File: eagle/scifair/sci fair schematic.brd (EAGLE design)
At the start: 45.4 x 80 mm, 19 parts, among them IC1 LM555N, IC2 LM340H-12, Q1 BC817-16W, Q2 BC817-16W, X1 RIGHT, X2 LEFT, X3 PWR

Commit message: Rework USB connections to use Sparkfun breakouts due to resource unavailability
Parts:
- removed X1: RIGHT, con-yamaichi:USB-A003
- removed X2: LEFT, con-yamaichi:USB-A003
- removed X3: PWR, con-yamaichi:USB-A003
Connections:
- net N$6 renamed 5V
- removed net N$1: C2.1, IC2.1, X1.4, X2.4, X3.3
- removed net N$2: F1.1, X2.3
- removed net N$3: F2.1, X1.3
- new net VCC: C2.1, F1.1, F2.1, IC2.1
- net GND: no longer X3.4
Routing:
- net N$1: track 97.1 -> 0.00 mm, vias 1 -> 0
- net VCC: track 0.00 -> 25.3 mm, vias 0 -> 2
- net N$2: track 15.5 -> 0.00 mm
- net N$3: track 12.9 -> 0.00 mm, vias 2 -> 0
- net GND: track 131.3 -> 122.6 mm, vias 7 -> 5
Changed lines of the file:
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@@
 <attribute name="VALUE" x="60.96" y="71.374" size="1.27" layer="27" ratio="10" rot="R90"/>
-</element>
-<element name="X1" library="con-yamaichi" package="USB-A003" value="RIGHT" x="107.95" y="35.56" smashed="yes" rot="R90">
-<attribute name="OC_FARNELL" value="unknown" x="107.95" y="35.56" size="1.778" layer="27" rot="R90" display="off"/>
-<attribute name="MPN" value="" x="107.95" y="35.56" size="1.778" layer="27" rot="R90" display="off"/>
-<attribute name="MF" value="" x="107.95" y="35.56" size="1.778" layer="27" rot="R90" display="off"/>
-<attribute name="OC_NEWARK" value="unknown" x="107.95" y="35.56" size="1.778" layer="27" rot="R90" display="off"/>
-<attribute name="NAME" x="96.52" y="27.94" size="1.27" layer="25" rot="R180"/>
-<attribute name="VALUE" x="99.06" y="45.72" size="1.27" layer="27" rot="R180"/>
-</element>
-<element name="X2" library="con-yamaichi" package="USB-A003" value="LEFT" x="107.95" y="57.15" smashed="yes" rot="R90">
-<attribute name="OC_FARNELL" value="unknown" x="107.95" y="57.15" size="1.778" layer="27" rot="R90" display="off"/>
-<attribute name="MPN" value="" x="107.95" y="57.15" size="1.778" layer="27" rot="R90" display="off"/>
-<attribute name="MF" value="" x="107.95" y="57.15" size="1.778" layer="27" rot="R90" display="off"/>
-<attribute name="OC_NEWARK" value="unknown" x="107.95" y="57.15" size="1.778" layer="27" rot="R90" display="off"/>
-<attribute name="NAME" x="96.52" y="49.53" size="1.27" layer="25" rot="R180"/>
-<attribute name="VALUE" x="96.52" y="66.04" size="1.27" layer="27" rot="R180"/>
-</element>
-<element name="X3" library="con-yamaichi" package="USB-A003" value="PWR" x="90.17" y="86.36" smashed="yes" rot="R180">
-<attribute name="OC_FARNELL" value="unknown" x="90.17" y="86.36" size="1.778" layer="27" rot="R180" display="off"/>
-<attribute name="MPN" value="" x="90.17" y="86.36" size="1.778" layer="27" rot="R180" display="off"/>
-<attribute name="MF" value="" x="90.17" y="86.36" size="1.778" layer="27" rot="R180" display="off"/>
-<attribute name="OC_NEWARK" value="unknown" x="90.17" y="86.36" size="1.778" layer="27" rot="R180" display="off"/>
-<attribute name="NAME" x="95.25" y="71.12" size="1.27" layer="25" rot="R270"/>
-<attribute name="VALUE" x="80.01" y="78.74" size="1.27" layer="27" rot="R270"/>
 </element>
 <element name="LED3" library="led" package="LED3MM" value="TLLY4400" x="87.63" y="60.96" smashed="yes">
@@
 </elements>
 <signals>
-<signal name="N$1">
-<contactref element="X3" pad="3"/>
-<contactref element="X1" pad="4"/>
-<contactref element="X2" pad="4"/>
-<contactref element="IC2" pad="1"/>
-<contactref element="C2" pad="1"/>
-<wire x1="74.93" y1="20.32" x2="74.93" y2="16.51" width="0.4064" layer="16"/>
-<wire x1="74.93" y1="16.51" x2="78.74" y2="16.51" width="0.4064" layer="16"/>
-<wire x1="78.74" y1="16.51" x2="81.915" y2="13.335" width="0.4064" layer="16"/>
-<wire x1="93.95" y1="39.06" x2="91.13" y2="39.06" width="0.4064" layer="1"/>
-<wire x1="91.13" y1="39.06" x2="91.44" y2="38.1" width="0.4064" layer="1"/>
-<wire x1="91.44" y1="38.1" x2="91.44" y2="21.59" width="0.4064" layer="1"/>
-<wire x1="91.44" y1="21.59" x2="81.915" y2="13.335" width="0.4064" layer="1"/>
-<via x="81.915" y="13.335" extent="1-16" drill="0.6" shape="square"/>
-<wire x1="81.915" y1="13.335" x2="85.09" y2="10.16" width="0.4064" layer="16"/>
-<wire x1="93.95" y1="60.65" x2="93.95" y2="64.8" width="0.4064" layer="1"/>
-<wire x1="93.95" y1="64.8" x2="88.9" y2="69.85" width="0.4064" layer="1"/>
-<wire x1="88.9" y1="69.85" x2="88.9" y2="72.09" width="0.4064" layer="1"/>
-<wire x1="88.9" y1="72.09" x2="89.17" y2="72.36" width="0.4064" layer="1"/>
-<wire x1="93.95" y1="60.65" x2="96.83" y2="60.65" width="0.4064" layer="1"/>
-<wire x1="96.83" y1="60.65" x2="100.33" y2="57.15" width="0.4064" layer="1"/>
-<wire x1="100.33" y1="57.15" x2="100.33" y2="38.1" width="0.4064" layer="1"/>
-<wire x1="100.33" y1="38.1" x2="94.91" y2="38.1" width="0.4064" layer="1"/>
-<wire x1="94.91" y1="38.1" x2="93.95" y2="39.06" width="0.4064" layer="1"/>
-</signal>
-<signal name="N$2">
-<contactref element="X2" pad="3"/>
-<contactref element="F1" pad="1"/>
-<wire x1="93.95" y1="58.15" x2="91.17" y2="58.15" width="0.4064" layer="1"/>
-<wire x1="91.17" y1="58.15" x2="90.17" y2="57.15" width="0.4064" layer="1"/>
-<wire x1="90.17" y1="57.15" x2="90.17" y2="45.85" width="0.4064" layer="1"/>
-</signal>
-<signal name="N$3">
-<contactref element="X1" pad="3"/>
-<contactref element="F2" pad="1"/>
-<wire x1="93.95" y1="36.56" x2="94.22" y2="36.83" width="0.4064" layer="1"/>
-<wire x1="94.22" y1="36.83" x2="97.79" y2="36.83" width="0.4064" layer="1"/>
-<via x="97.79" y="36.83" extent="1-16" drill="0.6" shape="square"/>
-<via x="93.98" y="40.64" extent="1-16" drill="0.6" shape="square"/>
-<wire x1="93.98" y1="40.64" x2="93.98" y2="43.05" width="0.4064" layer="1"/>
-<wire x1="93.98" y1="40.64" x2="97.79" y2="39.37" width="0.4064" layer="16"/>
-<wire x1="97.79" y1="39.37" x2="97.79" y2="36.83" width="0.4064" layer="16"/>
-</signal>
 <signal name="N$4">
 <contactref element="Q1" pad="2"/>
@@
 </signal>
 <signal name="GND">
-<contactref element="X3" pad="4"/>
 <contactref element="IC2" pad="2"/>
 <contactref element="C2" pad="2"/>
@@
 <wire x1="77.47" y1="75.6412" x2="77.47" y2="71.12" width="0.4064" layer="16"/>
 <via x="77.47" y="71.12" extent="1-16" drill="0.6" shape="square"/>
-<wire x1="85.43" y1="71.12" x2="86.67" y2="72.36" width="0.4064" layer="1"/>
 <wire x1="68.58" y1="36.83" x2="66.294" y2="36.83" width="0.4064" layer="16"/>
 <wire x1="66.294" y1="36.83" x2="62.484" y2="33.02" width="0.4064" layer="16"/>
@@
 <wire x1="87.63" y1="17.78" x2="85.09" y2="20.32" width="0.4064" layer="16"/>
 <wire x1="85.09" y1="20.32" x2="80.01" y2="20.32" width="0.4064" layer="16"/>
-<wire x1="86.67" y1="72.36" x2="86.67" y2="69.54" width="0.4064" layer="1"/>
 <wire x1="86.67" y1="69.54" x2="88.9" y2="67.31" width="0.4064" layer="1"/>
 <via x="88.9" y="67.31" extent="1-16" drill="0.6" shape="square"/>
@@
 <via x="81.28" y="54.61" extent="1-16" drill="0.6" shape="square"/>
 <wire x1="81.28" y1="54.61" x2="81.28" y2="57.15" width="0.4064" layer="16"/>
-<via x="81.28" y="71.12" extent="1-16" drill="0.6" shape="square"/>
-<wire x1="81.28" y1="71.12" x2="77.47" y2="71.12" width="0" layer="19" extent="1-1"/>
-<wire x1="81.28" y1="71.12" x2="83.82" y2="71.12" width="0.4064" layer="16"/>
-<via x="83.82" y="71.12" extent="1-16" drill="0.6" shape="square"/>
-<wire x1="83.82" y1="71.12" x2="85.43" y2="71.12" width="0.4064" layer="1"/>
-</signal>
-<signal name="N$6">
+<wire x1="86.67" y1="69.54" x2="77.47" y2="71.12" width="0" layer="19" extent="1-1"/>
+</signal>
+<signal name="5V">
 <contactref element="IC2" pad="3"/>
 <contactref element="C3" pad="1"/>
@@
 <wire x1="86.36" y1="60.96" x2="86.36" y2="64.77" width="0.4064" layer="16"/>
 </signal>
+<signal name="VCC">
+<contactref element="C2" pad="1"/>
+<contactref element="IC2" pad="1"/>
+<contactref element="F2" pad="1"/>
+<wire x1="94.22" y1="36.83" x2="97.79" y2="36.83" width="0.4064" layer="1"/>
+<via x="97.79" y="36.83" extent="1-16" drill="0.6" shape="square"/>
+<via x="93.98" y="40.64" extent="1-16" drill="0.6" shape="square"/>
+<wire x1="93.98" y1="40.64" x2="93.98" y2="43.05" width="0.4064" layer="1"/>
+<wire x1="93.98" y1="40.64" x2="97.79" y2="39.37" width="0.4064" layer="16"/>
+<wire x1="97.79" y1="39.37" x2="97.79" y2="36.83" width="0.4064" layer="16"/>
+<contactref element="F1" pad="1"/>
+<wire x1="91.17" y1="58.15" x2="90.17" y2="57.15" width="0.4064" layer="1"/>
+<wire x1="90.17" y1="57.15" x2="90.17" y2="45.85" width="0.4064" layer="1"/>
+<wire x1="93.98" y1="43.05" x2="90.17" y2="45.85" width="0" layer="19" extent="1-1"/>
+<wire x1="74.93" y1="20.32" x2="94.22" y2="36.83" width="0" layer="19" extent="1-1"/>
+<wire x1="85.09" y1="10.16" x2="74.93" y2="20.32" width="0" layer="19" extent="1-1"/>
+</signal>
 </signals>

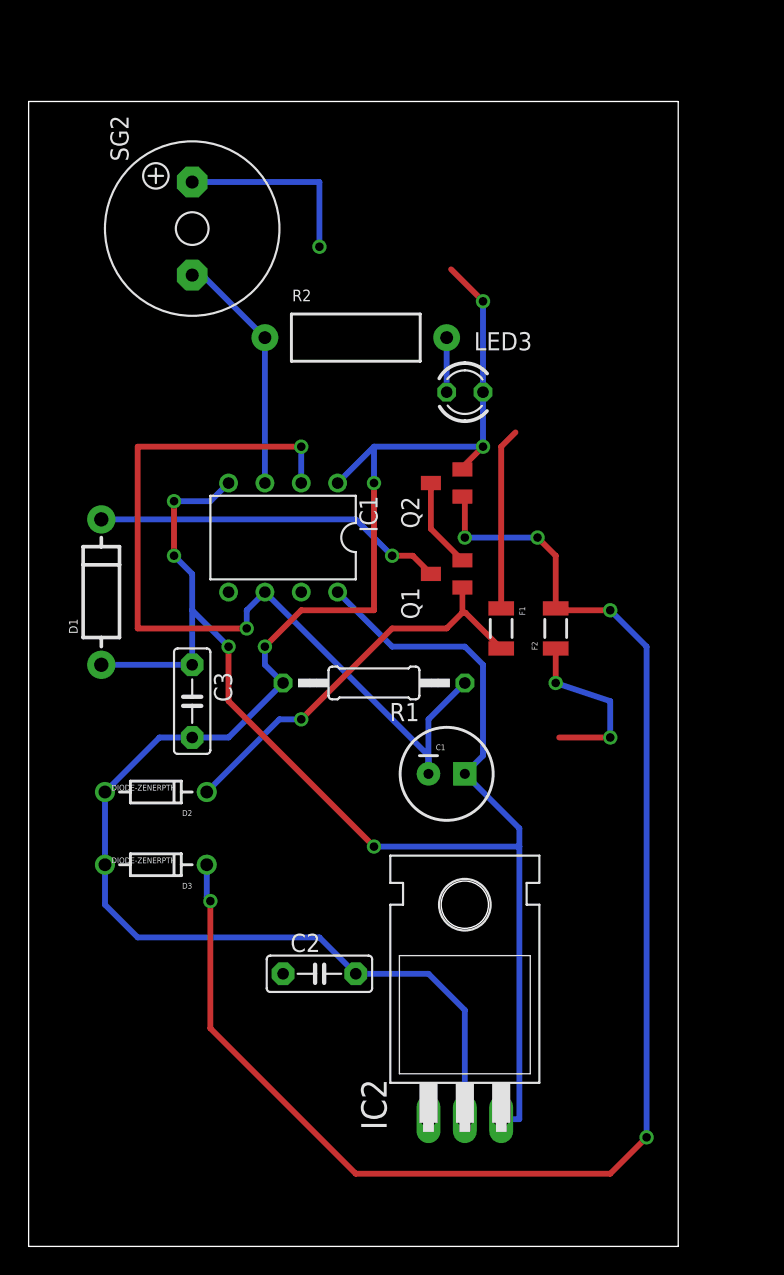
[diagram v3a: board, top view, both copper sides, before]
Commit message: Rework board with copper pours and SparkFun USB breakout compatibility
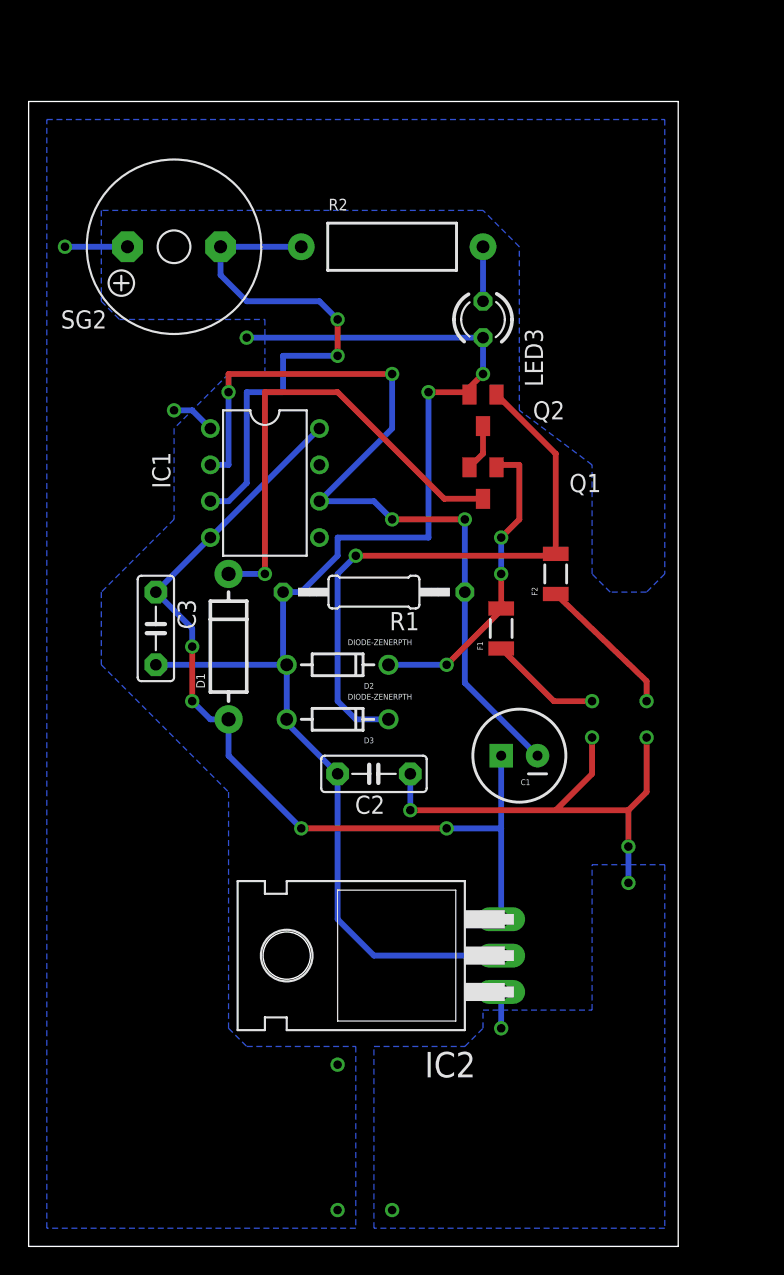
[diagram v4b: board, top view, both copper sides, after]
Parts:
- moved D3 16.3 mm to (78.7, 38.1)
- moved D2 15.5 mm to (78.7, 41.9)
- moved C2 14.5 mm to (81.3, 34.3), turned to 180 degrees
- moved D1 9.67 mm to (71.1, 43.2)
- moved IC2 7.73 mm to (80.0, 21.6), turned to 90 degrees
- moved R2 6.84 mm to (82.5, 71.1)
- moved Q1 6.84 mm to (88.9, 54.6), turned to 180 degrees
- moved R1 6.35 mm to (81.3, 47.0)
- moved C3 5.68 mm to (66.0, 44.5)
- moved Q2 5.68 mm to (88.9, 59.7), turned to 180 degrees
- moved LED3 5.24 mm to (88.9, 66.0), turned to 270 degrees
- moved C1 5.24 mm to (91.4, 35.6), turned to 180 degrees
- moved IC1 4.02 mm to (73.7, 54.6), turned to 270 degrees
- moved F2 3.81 mm to (94.0, 48.3)
- moved SG2 1.80 mm to (67.3, 71.1), turned to 180 degrees
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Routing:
- net N$9: track 102.5 -> 41.6 mm, vias 5 -> 1
- net 5V: track 102.0 -> 63.0 mm
- net VCC: track 25.3 -> 55.2 mm, vias 2 -> 9
- net GND: track 122.6 -> 100.0 mm, vias 5 -> 6
- net N$10: track 17.0 -> 37.9 mm, vias 0 -> 2
- net N$7: track 24.6 -> 33.6 mm
- net N$8: track 28.6 -> 21.8 mm, vias 1 -> 3
- net N$4: track 6.31 -> 3.27 mm
- net N$11: track 62.2 -> 59.3 mm, vias 2 -> 4
- added copper zone on layer 16, net GND
- added copper zone on layer 16, net VCC

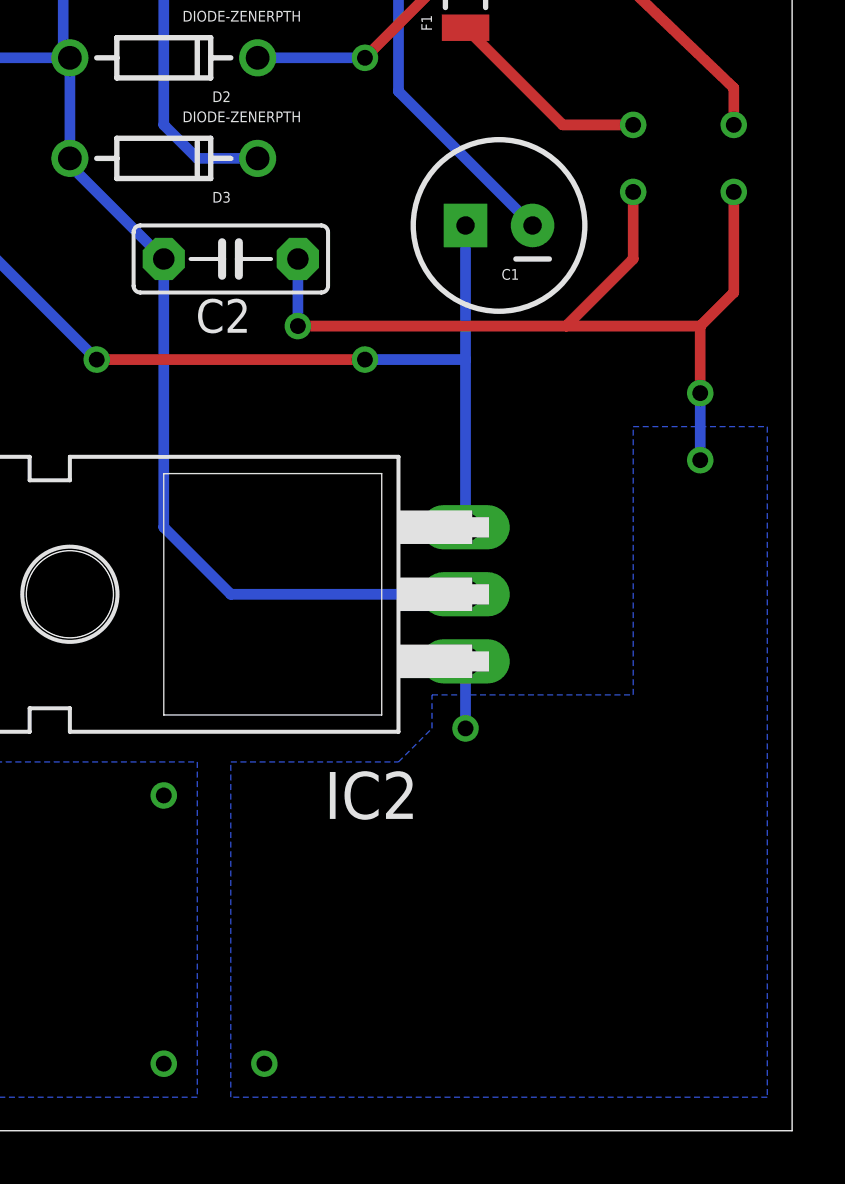
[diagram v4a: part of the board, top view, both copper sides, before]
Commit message: Add extra copper pours for increased etching efficiency
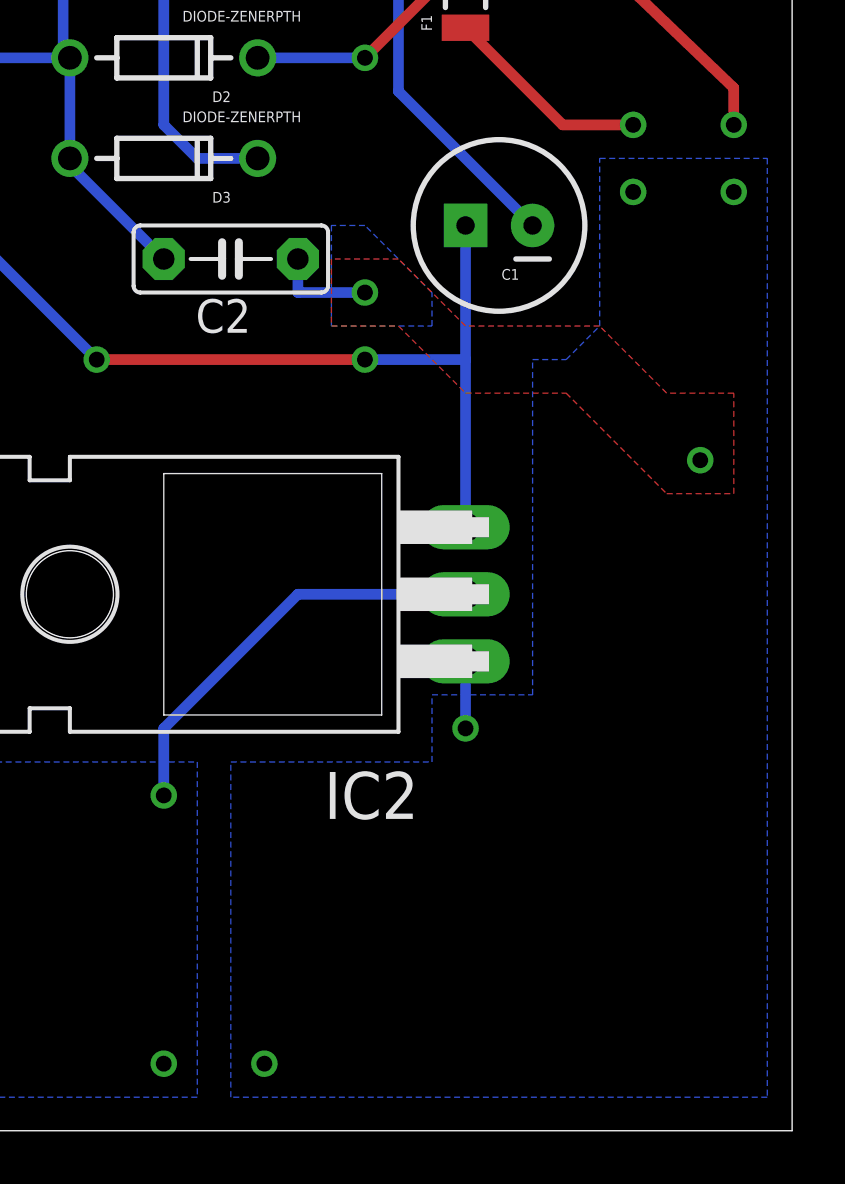
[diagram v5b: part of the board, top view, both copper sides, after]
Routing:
- net VCC: track 55.2 -> 24.4 mm, vias 9 -> 8
- net GND: track 100.0 -> 93.4 mm, vias 6 -> 7
- added copper zone on layer 1, net VCC
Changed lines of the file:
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@@
 </polygon>
 <via x="78.74" y="3.81" extent="1-16" drill="0.6" shape="square"/>
-<wire x1="90.17" y1="21.59" x2="81.28" y2="21.59" width="0.4064" layer="16"/>
-<wire x1="81.28" y1="21.59" x2="78.74" y2="24.13" width="0.4064" layer="16"/>
-<wire x1="78.74" y1="24.13" x2="78.74" y2="34.29" width="0.4064" layer="16"/>
 <wire x1="75.184" y1="38.1" x2="75.184" y2="37.846" width="0.4064" layer="16"/>
 <wire x1="75.184" y1="37.846" x2="78.74" y2="34.29" width="0.4064" layer="16"/>
@@
 <wire x1="78.74" y1="50.8" x2="85.09" y2="50.8" width="0.4064" layer="16"/>
 <wire x1="85.09" y1="50.8" x2="85.09" y2="60.96" width="0.4064" layer="16"/>
+<via x="78.74" y="13.97" extent="1-16" drill="0.6" shape="square"/>
+<wire x1="90.17" y1="21.59" x2="83.82" y2="21.59" width="0.4064" layer="16"/>
+<wire x1="83.82" y1="21.59" x2="78.74" y2="16.51" width="0.4064" layer="16"/>
+<wire x1="78.74" y1="16.51" x2="78.74" y2="13.97" width="0.4064" layer="16"/>
 </signal>
 <signal name="5V">
@@
 <contactref element="F1" pad="1"/>
 <via x="96.52" y="39.37" extent="1-16" drill="0.6" shape="square"/>
-<via x="96.52" y="36.83" extent="1-16" drill="0.6" shape="square"/>
 <via x="100.33" y="39.37" extent="1-16" drill="0.6" shape="square"/>
-<via x="100.33" y="36.83" extent="1-16" drill="0.6" shape="square"/>
 <wire x1="96.52" y1="39.37" x2="93.85" y2="39.37" width="0.4064" layer="1"/>
 <wire x1="93.85" y1="39.37" x2="90.17" y2="43.05" width="0.4064" layer="1"/>
 <wire x1="100.33" y1="39.37" x2="100.33" y2="40.77" width="0.4064" layer="1"/>
 <wire x1="100.33" y1="40.77" x2="93.98" y2="46.86" width="0.4064" layer="1"/>
-<wire x1="96.52" y1="36.83" x2="96.52" y2="34.29" width="0.4064" layer="1"/>
-<wire x1="96.52" y1="34.29" x2="93.98" y2="31.75" width="0.4064" layer="1"/>
-<wire x1="100.33" y1="36.83" x2="100.33" y2="33.02" width="0.4064" layer="1"/>
-<wire x1="100.33" y1="33.02" x2="99.06" y2="31.75" width="0.4064" layer="1"/>
-<wire x1="99.06" y1="31.75" x2="93.98" y2="31.75" width="0.4064" layer="1"/>
-<wire x1="93.98" y1="31.75" x2="83.82" y2="31.75" width="0.4064" layer="1"/>
-<via x="83.82" y="31.75" extent="1-16" drill="0.6" shape="square"/>
-<wire x1="83.82" y1="31.75" x2="83.82" y2="34.29" width="0.4064" layer="16"/>
 <polygon width="0.4064" layer="16">
 <vertex x="81.28" y="2.54"/>
 <vertex x="81.28" y="15.24"/>
-<vertex x="87.63" y="15.24"/>
-<vertex x="88.9" y="16.51"/>
+<vertex x="88.9" y="15.24"/>
 <vertex x="88.9" y="17.78"/>
-<vertex x="96.52" y="17.78"/>
-<vertex x="96.52" y="27.94"/>
-<vertex x="101.6" y="27.94"/>
+<vertex x="92.71" y="17.78"/>
+<vertex x="92.71" y="30.48"/>
+<vertex x="93.98" y="30.48"/>
+<vertex x="95.25" y="31.75"/>
+<vertex x="95.25" y="38.1"/>
+<vertex x="101.6" y="38.1"/>
 <vertex x="101.6" y="2.54"/>
 </polygon>
-<via x="99.06" y="29.21" extent="1-16" drill="0.6" shape="square"/>
-<wire x1="99.06" y1="29.21" x2="99.06" y2="31.75" width="0.4064" layer="1"/>
 <via x="82.55" y="3.81" extent="1-16" drill="0.6" shape="square"/>
 <via x="90.17" y="16.51" extent="1-16" drill="0.6" shape="square"/>
 <wire x1="90.17" y1="16.51" x2="90.17" y2="19.05" width="0.4064" layer="16"/>
 <via x="99.06" y="26.67" extent="1-16" drill="0.6" shape="square"/>
-<wire x1="99.06" y1="26.67" x2="99.06" y2="29.21" width="0.4064" layer="16"/>
+<via x="86.36" y="33.02" extent="1-16" drill="0.6" shape="square"/>
+<polygon width="0.4064" layer="16">
+<vertex x="85.09" y="35.56"/>
+<vertex x="85.09" y="31.75"/>
+<vertex x="88.9" y="31.75"/>
+<vertex x="88.9" y="33.02"/>
+<vertex x="86.36" y="35.56"/>
+</polygon>
+<polygon width="0.4064" layer="1">
+<vertex x="85.09" y="34.29"/>
+<vertex x="85.09" y="31.75"/>
+<vertex x="87.63" y="31.75"/>
+<vertex x="90.17" y="29.21"/>
+<vertex x="93.98" y="29.21"/>
+<vertex x="97.79" y="25.4"/>
+<vertex x="100.33" y="25.4"/>
+<vertex x="100.33" y="29.21"/>
+<vertex x="97.79" y="29.21"/>
+<vertex x="95.25" y="31.75"/>
+<vertex x="90.17" y="31.75"/>
+<vertex x="87.63" y="34.29"/>
+</polygon>
+<via x="96.52" y="36.83" extent="1-16" drill="0.6" shape="square"/>
+<via x="100.33" y="36.83" extent="1-16" drill="0.6" shape="square"/>
 <wire x1="100.33" y1="36.83" x2="100.33" y2="39.37" width="0" layer="19" extent="1-1"/>
 <wire x1="96.52" y1="39.37" x2="96.52" y2="36.83" width="0" layer="19" extent="1-1"/>
-</signal>
-<signal name="N$1">
-<via x="78.74" y="13.97" extent="1-16" drill="0.6" shape="square"/>
+<wire x1="86.36" y1="33.02" x2="83.82" y2="33.02" width="0.4064" layer="16"/>
+<wire x1="83.82" y1="33.02" x2="83.82" y2="34.29" width="0.4064" layer="16"/>
 </signal>
 </signals>
